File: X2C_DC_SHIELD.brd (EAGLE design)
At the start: 54.6 x 40.6 mm, 60 parts, among them CON1 X2C_PINHD-4X14_SMD, IC1 MCP16251, IC2 MCP6004ST, IC3 7408, T1 DMG6602SVT, T2 DMG6602SVT

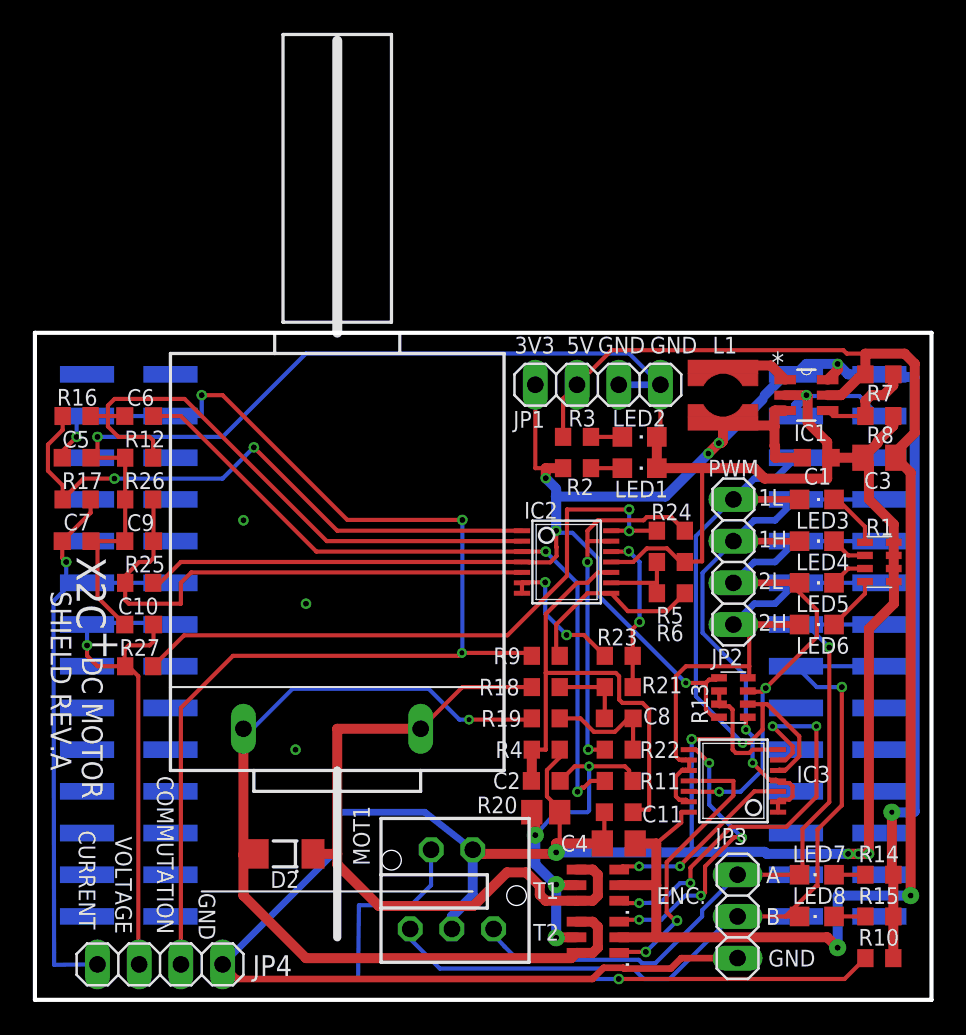
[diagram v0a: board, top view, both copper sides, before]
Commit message: Updated amplifier values
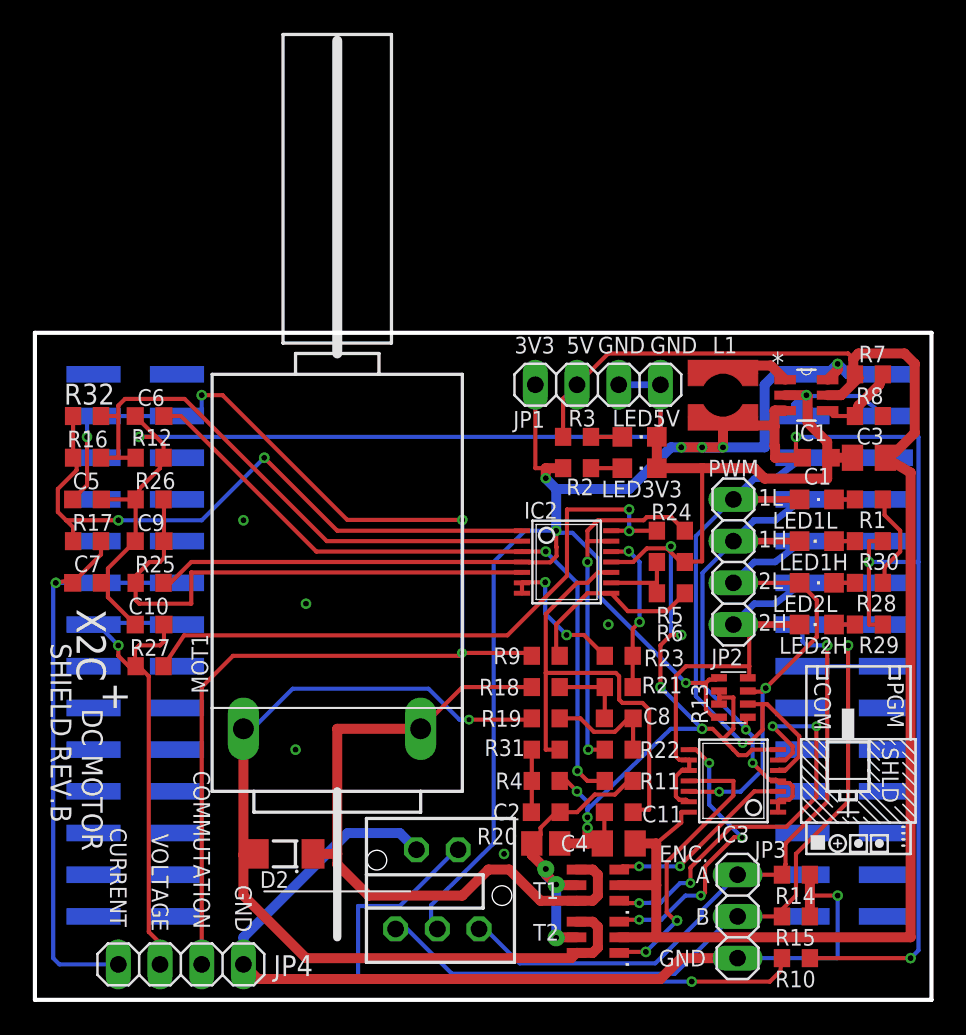
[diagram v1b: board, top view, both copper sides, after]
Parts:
- removed LED7, LED8: Green, KANDO_KOZOS:CHIPLED_0805
- added R28, R29, R30: 680R, KANDO_KOZOS_V2:R0603
- added R31: 2,2k, KANDO_KOZOS:R0603
- added R32: 68k 1%, KANDO_KOZOS_V2:R0603
- C10, C5, C7, C8: value 2,2nF -> 22nF; device KANDO_KOZOS:C0603K -> C_EU_Kando:C0603K
- C11: value 2,2nF -> 1uF; device KANDO_KOZOS:C0603K -> KANDO_KOZOS_V2:C0603K
- C3: device C_EU_Kando:C0805K -> KANDO_KOZOS:C0805K
- C6: value 2,2nF -> 4,7uF; device KANDO_KOZOS:C0603K -> C_EU_Kando:C0603K
- C9: value 100nF -> 1uF; device KANDO_KOZOS:C0603K -> C_EU_Kando:C0603K
- MOT1: device KANDO_KOZOS:DC_MOTOR -> KANDO_KOZOS_V2:DC_MOTOR
- R1: value 330R -> 680R; device KANDO_KOZOS:EXBV8V_A -> KANDO_KOZOS_V2:R0603
- R14, R15: value 330R -> 4,7k; device KANDO_KOZOS:R0603 -> R_EU:R0603
- R16, R21, R22: value 22k 1% -> 68k 1%; device KANDO_KOZOS:R0603 -> KANDO_KOZOS_V2:R0603
- R23, R24: value 2,2k -> 22k 1%; device KANDO_KOZOS:R0603 -> KANDO_KOZOS_V2:R0603
- R3: value 330R -> 680R; device KANDO_KOZOS:R0603 -> KANDO_KOZOS_V2:R0603
- R4: value 2,2k -> 330k 1%; device KANDO_KOZOS:R0603 -> KANDO_KOZOS_V2:R0603
- R6: value 68k 1% -> 330k 1%; device KANDO_KOZOS:R0603 -> KANDO_KOZOS_V2:R0603
- moved R10 5.08 mm to (46.4, 2.54)
- moved R14 5.08 mm to (46.4, 7.62)
- moved R15 5.08 mm to (46.4, 5.08)
- moved R1 3.86 mm to (50.8, 30.5), turned to 180 degrees
- moved C5 2.62 mm to (3.17, 30.5)
- moved C7 2.62 mm to (3.17, 25.4)
- moved R16 2.62 mm to (3.17, 33.0)
- moved R17 2.62 mm to (3.17, 27.9)
- moved C2 1.91 mm to (31.1, 11.4)
- moved R20 1.90 mm to (31.1, 9.53)
- moved R4 1.90 mm to (31.1, 13.3)
- moved JP4 1.27 mm to (8.89, 2.16)
- moved C3 0.64 mm to (50.8, 33.0)
- moved R7 0.64 mm to (50.8, 38.1)
- moved R8 0.64 mm to (50.8, 35.6)
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- renumbered LED1 to LED3V3, LED2 to LED5V, LED3 to LED1L, LED4 to LED1H, LED5 to LED2L, LED6 to LED2H
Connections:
- removed net N$11: C6.2, IC2.2, R12.2, R16.1
- net +3V3: now also MOT1.EMIT, R29.1, R30.1; no longer R14.2, R15.2
- net GND: now also C6.2, MOT1.A, R1.1, R14.2, R15.2, R28.1; no longer MOT1.C, MOT1.EMIT, R1.5, R1.6, R1.7, R1.8
- net IMOTOR: now also R32.2
- net N$10: now also R1.2; no longer R1.1
- net N$13: now also LED1H.A, R30.2; no longer LED1H.C, R1.2
- net N$14: now also R28.2; no longer R1.3
- net N$15: now also IC2.2, R12.2, R16.1, R32.1; no longer LED2H.C, R1.4
- net N$16: now also C2.1, R31.2, R4.2; no longer LED8.A, R15.1
- net N$26: now also R31.1; no longer C2.1, R4.2
- net N$28: now also MOT1.C; no longer MOT1.A
- net N$6: now also LED2H.A, R29.2; no longer LED7.A, R14.1
- net PWM1H: now also LED1H.C; no longer LED1H.A
- net PWM2H: now also LED2H.C; no longer LED2H.A
- net QE_A: now also R14.1; no longer LED7.C
- net QE_B: now also R15.1; no longer LED8.C
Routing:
- net +3V3: track 131.0 -> 183.3 mm, vias 7 -> 10
- net N$11: track 36.8 -> 0.00 mm
- net GND: track 243.8 -> 209.2 mm, vias 10 -> 15
- net N$15: track 3.39 -> 34.7 mm
- net SHUNT: track 23.2 -> 18.1 mm, vias 4 -> 3
- net N$28: track 43.0 -> 38.9 mm
- net IMOTOR: track 37.2 -> 40.2 mm
- net N$26: track 31.4 -> 29.3 mm
- net N$22: track 44.7 -> 42.8 mm
- net N$16: track 1.91 -> 3.82 mm
- net N$10: track 3.52 -> 1.66 mm
- net COMMUTATION: track 77.7 -> 79.0 mm
- net N$12: track 6.13 -> 4.94 mm
- net N$14: track 2.24 -> 1.28 mm
- net N$13: track 2.24 -> 1.28 mm
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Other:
- board text added: "COM"
- board text added: "DC MOTOR SHIELD REV.B"
- board text added: "PGM"
- board text added: "SHLD"
- board text added: "http://x2c.microstickplus.com"
- board text removed: "DC MOTOR SHIELD REV.A"
- board text removed: "mark.wendler@gmail.com"
